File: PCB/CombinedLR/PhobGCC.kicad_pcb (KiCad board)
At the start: 2 copper layers, 143 x 91.4 mm, 76 parts, among them J1 Conn_01x06_Female, J2 Conn_01x04_Female, J3 Conn_01x01_Male, J4 Conn_01x04_Male, J5 Conn_01x02_Male, Q1 Q_NMOS_GSD, Q2 Q_PMOS_GDS, Q3 Q_NMOS_GSD, SW1 A, SW10 Dup, SW11 Dright, SW12 Ddown, SW2 B, SW3 X, SW4 Y, SW5 Start, SW6 L, SW7 R, SW8 1825027-5, SW9 Dleft, U1 Teensy4.0, U2 2x DRV5053CAQLPGM Hall Effect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, U3 GP2S60-MFG, U4 GP2S60-MFG, U5 Stickbox_Assembly

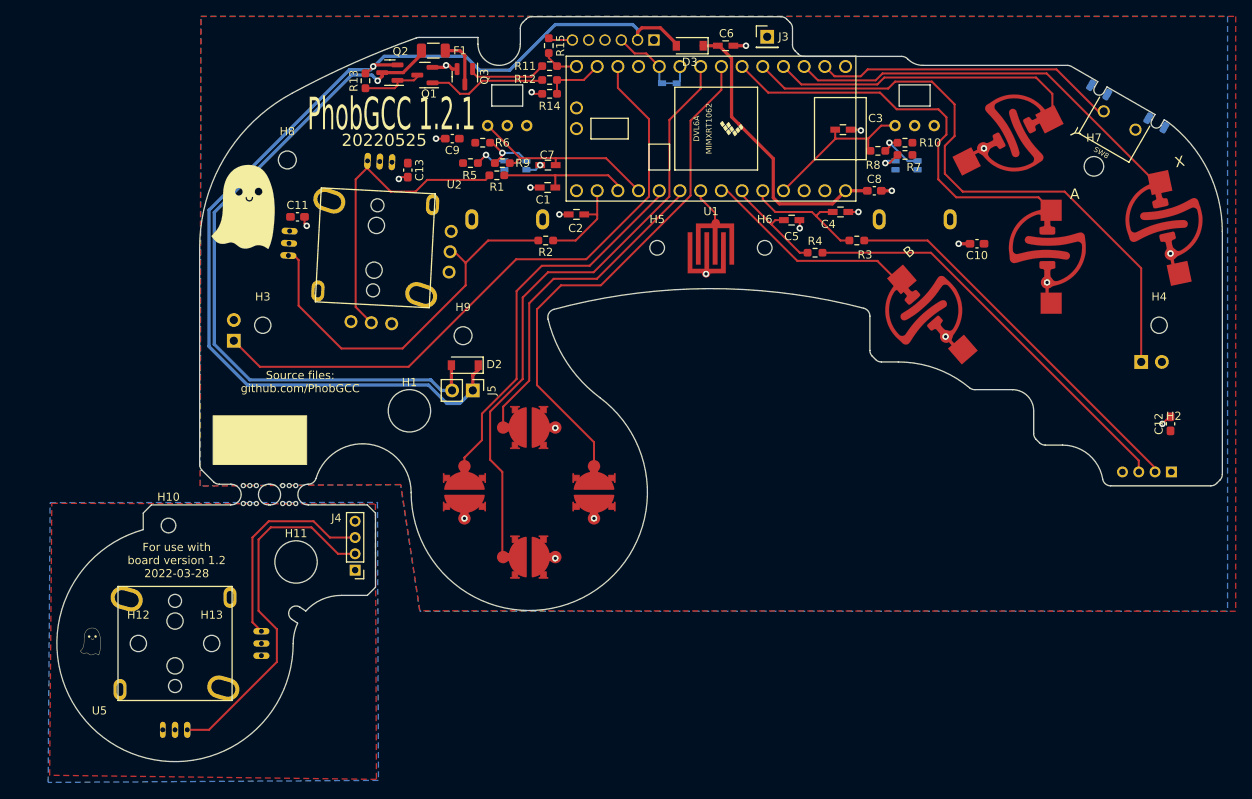
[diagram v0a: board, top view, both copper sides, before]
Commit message: fixed LR
working on mouseclick LR boards.
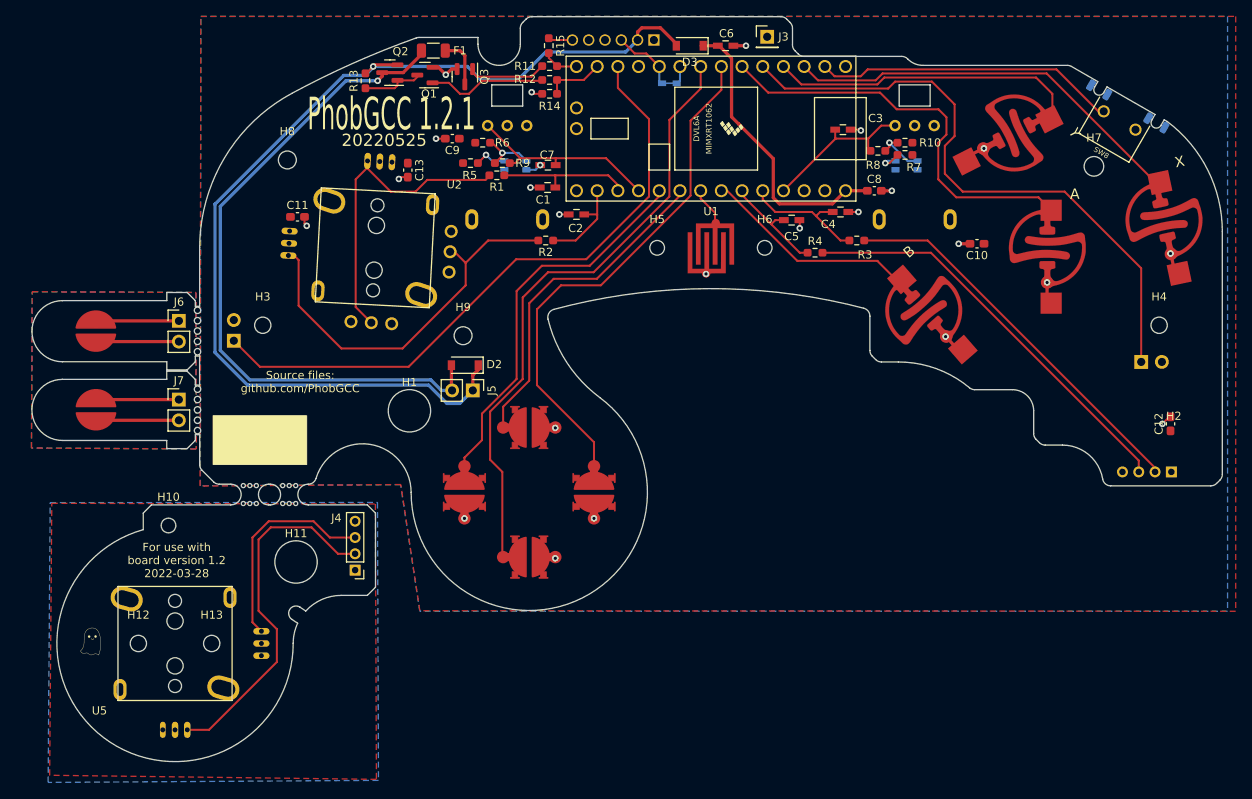
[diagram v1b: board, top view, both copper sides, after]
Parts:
- removed the G*** at (55.4, 73.5)
- added H17: MouseBiteRB, PhobGCC_Footprints:breakaway-mousebites, F.Cu at (49.8, 98.3)
- added H17: MouseBiteRB, PhobGCC_Footprints:breakaway-mousebites, F.Cu at (49.8, 88.6)
- added J6: Conn_01x02_Male, Connector_PinHeader_2.54mm:PinHeader_1x02_P2.54mm_Vertical, F.Cu at (47.3, 87.4)
- added J7: Conn_01x02_Male, Connector_PinHeader_2.54mm:PinHeader_1x02_P2.54mm_Vertical, F.Cu at (47.3, 97.0)
- added SW13: LB, PhobGCC_Footprints:Trigger_Contact, F.Cu at (37.1, 88.6)
- added SW14: RB, PhobGCC_Footprints:Trigger_Contact, F.Cu at (37.1, 98.3)
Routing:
- net Net-(J6-Pad2): track 0.00 -> 10.5 mm
- net Net-(J6-Pad1): track 0.00 -> 10.5 mm
- net Net-(J7-Pad2): track 0.00 -> 10.5 mm
- net Net-(J7-Pad1): track 0.00 -> 10.4 mm
- net +5V: track 132.4 -> 129.5 mm
- net Net-(D2-Pad2): track 85.0 -> 83.8 mm
- added copper zone on B.Cu, net (none)
- added copper zone on F.Cu, net (none)
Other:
- board size 143 x 91.4 mm -> 146.1 x 91.4 mm

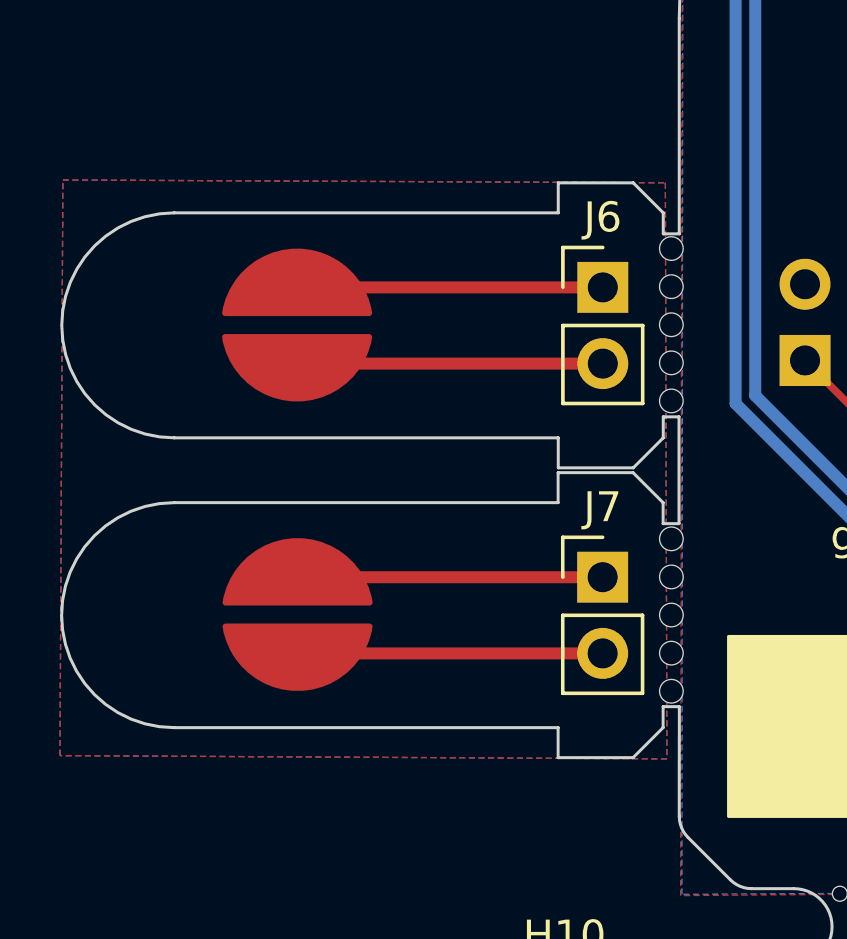
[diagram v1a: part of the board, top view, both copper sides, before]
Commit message: fixed LR board mouse switch footprint
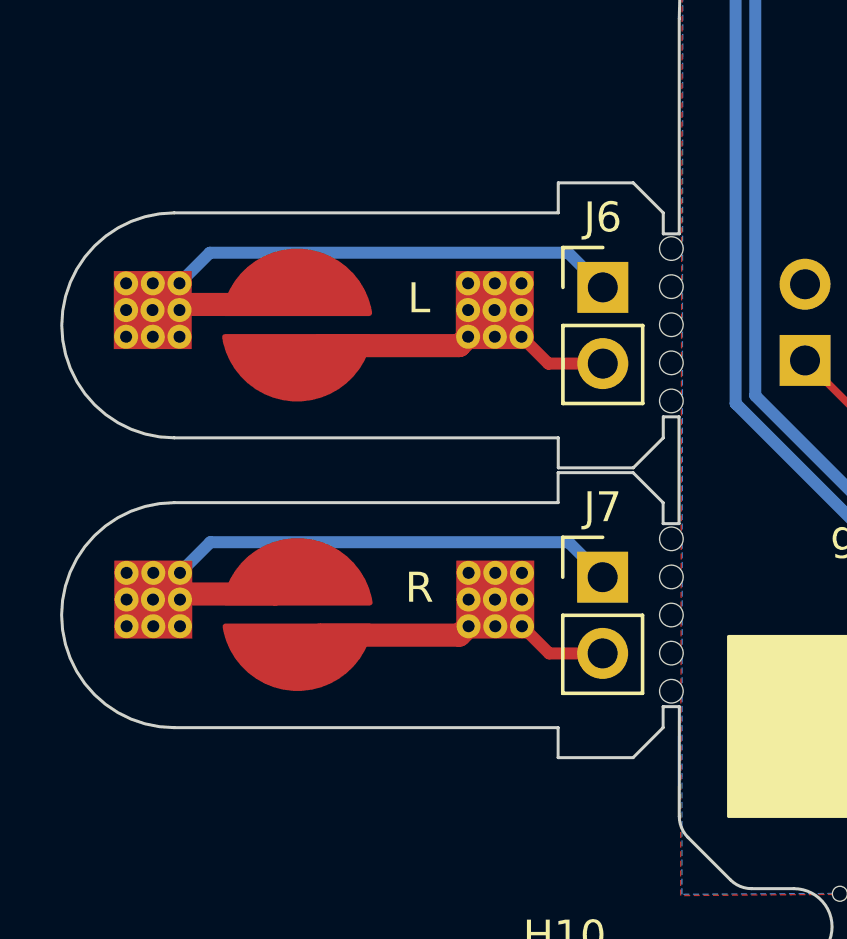
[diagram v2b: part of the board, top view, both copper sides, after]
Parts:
- H16: renamed from H17; value MouseBiteRB -> MouseBiteLB
- SW13: value LB -> L
- SW14: value RB -> R
- turned SW13 to 0 degrees
- turned SW14 to 0 degrees
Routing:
- net Net-(J7-Pad1): track 10.4 -> 21.5 mm
- net Net-(J6-Pad1): track 10.5 -> 21.5 mm
- net Net-(J7-Pad2): track 10.5 -> 11.7 mm
- net Net-(J6-Pad2): track 10.5 -> 11.7 mm
- removed copper zone on B.Cu, net (none)
- removed copper zone on F.Cu, net (none)

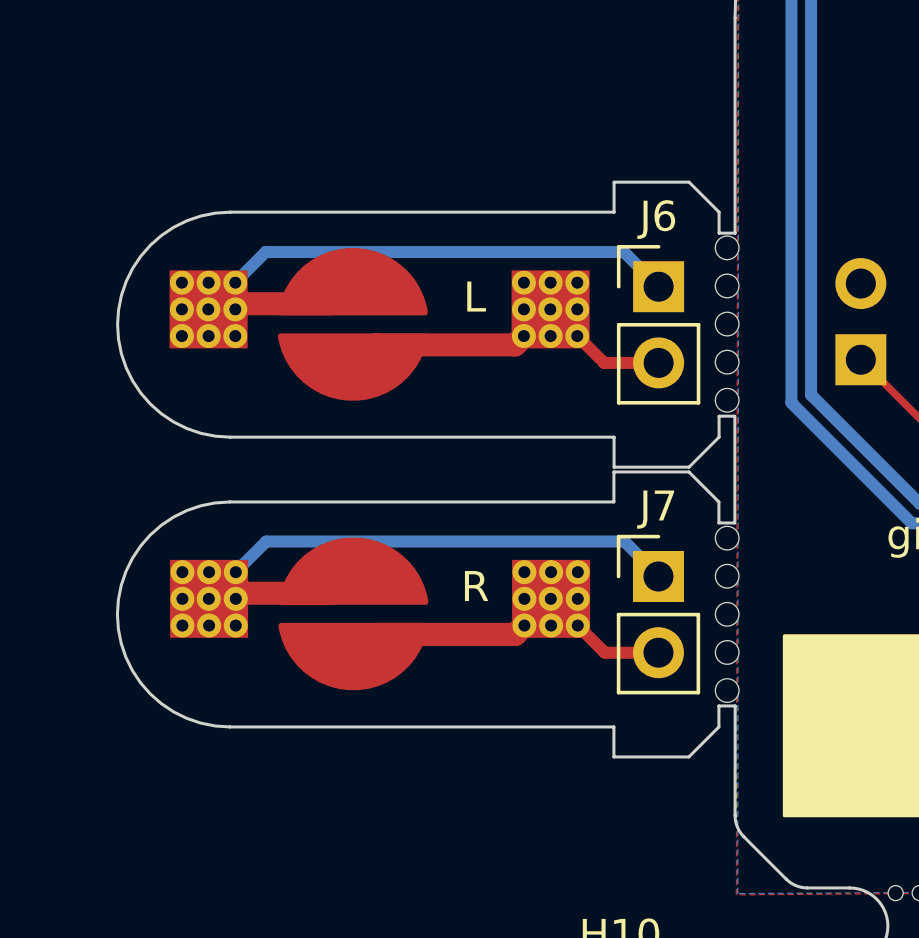
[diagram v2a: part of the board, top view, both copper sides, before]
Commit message: flipped trigger boards
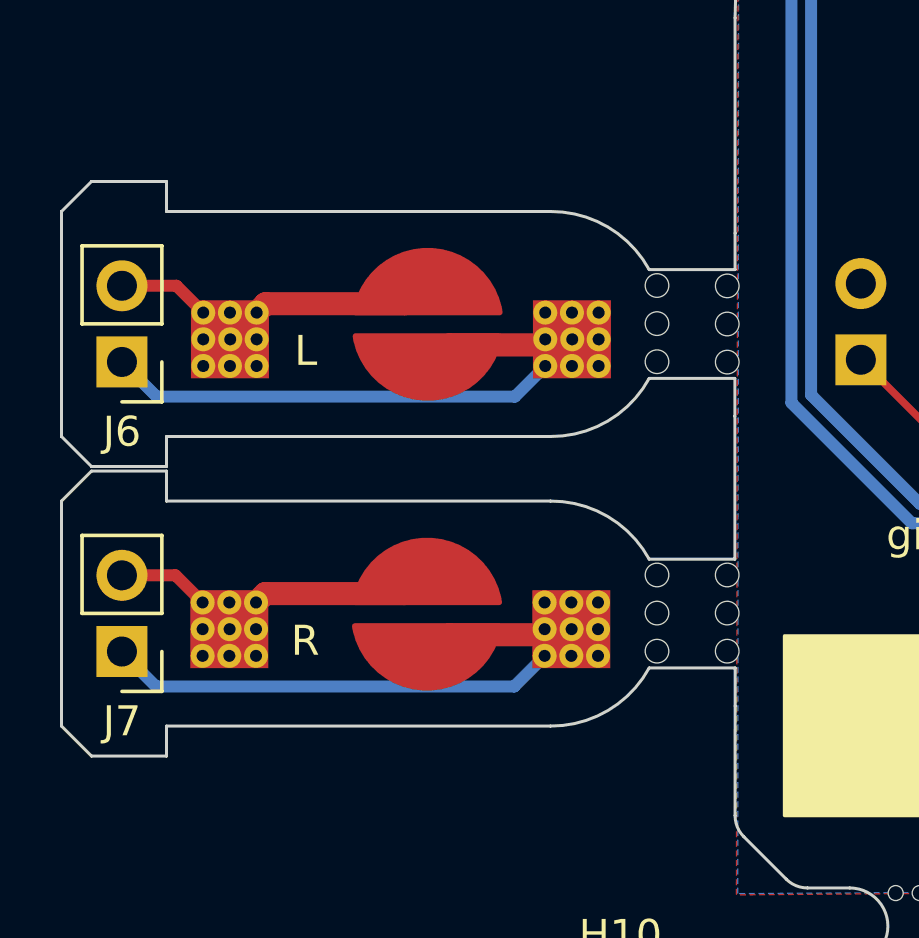
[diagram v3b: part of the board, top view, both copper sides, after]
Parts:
- added H17: MouseBiteLB, PhobGCC_Footprints:breakaway-mousebites, F.Cu at (49.9, 88.6)
- added H19: MouseBiteRB, PhobGCC_Footprints:breakaway-mousebites, F.Cu at (49.8, 98.2)
- H16: value MouseBiteLB -> MouseBiteLA
- H18: renamed from H17; value MouseBiteRB -> MouseBiteRA
- moved J6 18.1 mm to (29.4, 89.9), turned to 180 degrees
- moved J7 18.1 mm to (29.4, 99.5), turned to 180 degrees
- moved H18 2.85 mm to (47.0, 98.2), turned to -90 degrees
- moved H16 2.85 mm to (47.0, 88.6), turned to -90 degrees
- moved SW13 2.49 mm to (39.6, 88.6), turned to 180 degrees
- moved SW14 2.45 mm to (39.6, 98.3), turned to 180 degrees
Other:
- board size 146.1 x 91.4 mm -> 148 x 91.4 mm
- board text added: "MouseBiteLA"

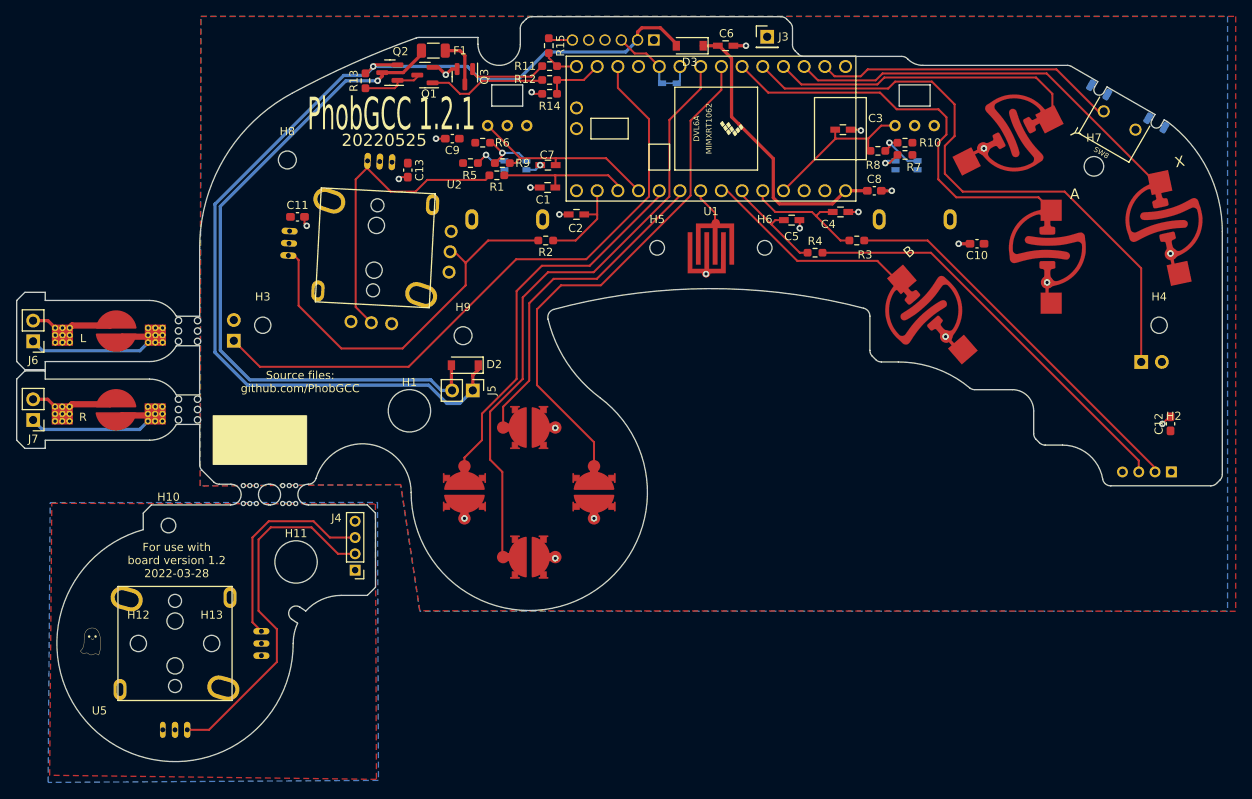
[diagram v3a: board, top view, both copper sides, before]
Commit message: swapped fuse, fixed LR
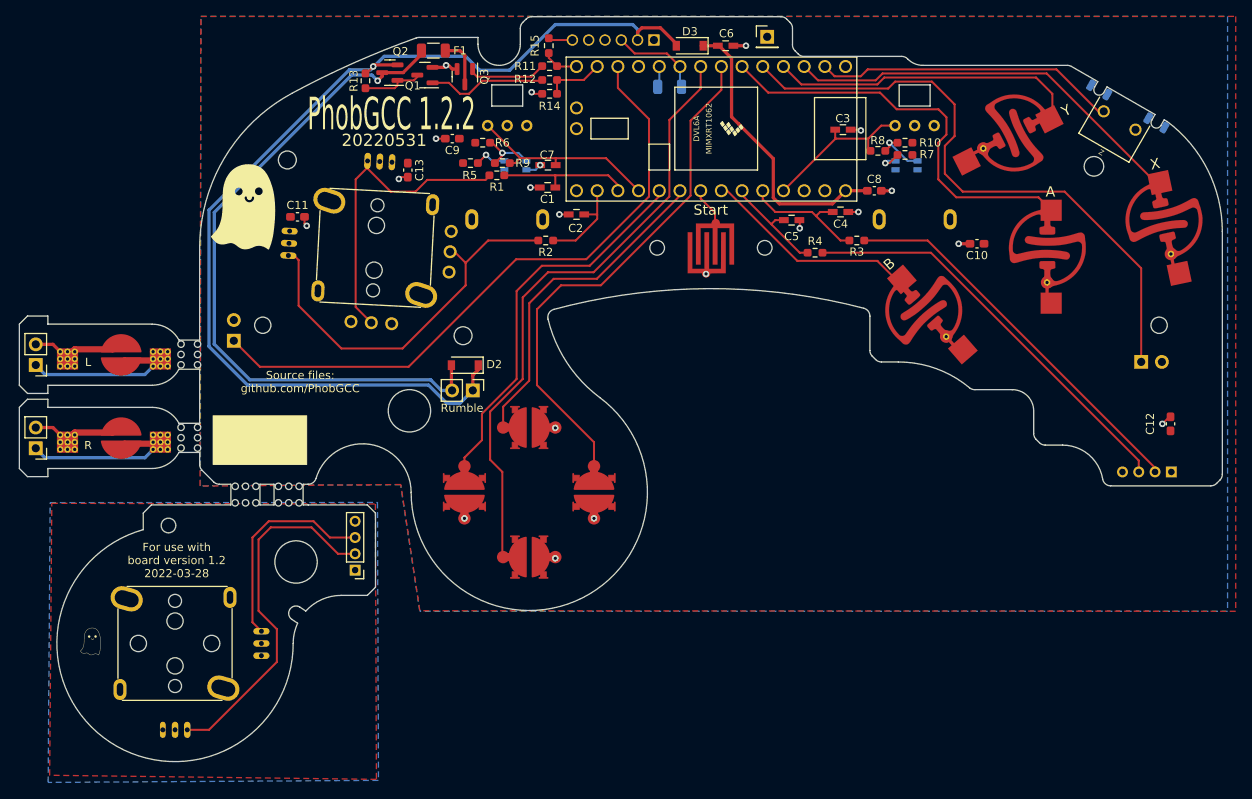
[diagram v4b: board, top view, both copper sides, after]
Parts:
- removed D1: D_Schottky_Shorted, Gamecube MB:D_SOD-523_Shorted
- removed H18: MouseBiteRA, PhobGCC_Footprints:breakaway-mousebites
- removed H19: MouseBiteRB, PhobGCC_Footprints:breakaway-mousebites
- added F2: Fuse, Resistor_SMD:R_1206_3216Metric, B.Cu at (107.5, 58.6)
- added G***: LOGO, PhobGCC_Footprints:Ghost Logo 2, F.Cu at (55.4, 73.5)
- H14, H15: footprint PhobGCC_Footprints:mouse-bite-2.54mm-slot -> PhobGCC_Footprints:breakaway-mousebites-double
- H16: footprint PhobGCC_Footprints:breakaway-mousebites -> PhobGCC_Footprints:breakaway-mousebites-double
- H17: value MouseBiteLB -> MouseBiteRA; footprint PhobGCC_Footprints:breakaway-mousebites -> PhobGCC_Footprints:breakaway-mousebites-double
- J5: value Conn_01x02_Male -> Rumble; footprint Connector_PinHeader_2.54mm:PinHeader_1x02_P2.54mm_Vertical -> PhobGCC_Footprints:Pin_Header_Straight_1x02_Pitch2.54mm
- J6: value Conn_01x02_Male -> L; footprint Connector_PinHeader_2.54mm:PinHeader_1x02_P2.54mm_Vertical -> PhobGCC_Footprints:Pin_Header_Straight_1x02_Pitch2.54mm
- J7: value Conn_01x02_Male -> R; footprint Connector_PinHeader_2.54mm:PinHeader_1x02_P2.54mm_Vertical -> PhobGCC_Footprints:Pin_Header_Straight_1x02_Pitch2.54mm
- SW6, SW7: footprint Pin_Headers:Pin_Header_Straight_1x02_Pitch2.54mm -> PhobGCC_Footprints:Pin_Header_Straight_1x02_Pitch2.54mm
- SW8: value 1825027-5 -> Z
- U1: footprint teensy:Teensy40_Edge_Pins -> PhobGCC_Footprints:Teensy40_Edge_Pins
- moved H16 13.4 mm to (49.9, 101.7), turned to 90 degrees
- moved H14 8.10 mm to (55.5, 109.9)
- moved SW14 3.53 mm to (40.2, 101.8)
- moved H15 3.53 mm to (60.8, 109.9)
- moved J7 3.49 mm to (29.7, 103.0)
- moved SW13 2.98 mm to (40.2, 91.5)
- moved J6 2.93 mm to (29.7, 92.8)
- moved H17 2.88 mm to (49.9, 91.5)
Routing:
- net /Data: track 8.17 -> 11.1 mm
- net +5V: track 129.5 -> 132.4 mm
- net Net-(D2-Pad2): track 83.8 -> 85.0 mm
- net GND: track 24.3 -> 23.9 mm, vias 24 -> 20
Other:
- board size 148 x 91.4 mm -> 147.6 x 91.4 mm
- board text added: "20220531"
- board text added: "MouseBiteRA"
- board text added: "PhobGCC 1.2.2"
- board text removed: "20220525"
- board text removed: "PhobGCC 1.2.1"
